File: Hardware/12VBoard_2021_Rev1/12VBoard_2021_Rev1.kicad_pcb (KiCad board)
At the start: 2 copper layers, 101.6 x 129.4 mm, 155 parts, among them Q10 IRLML2060, Q11 IRLML2060, Q12 IRLML2060, Q13 IRLML2060, Q3 IRLML2060, Q8 IRLML2060, Q9 IRLML2060, U1 LT1910, U10 INA198, U11 FDS66900AS, U12 LT1910, U13 INA198, U14 LT1910, U15 LT1910, U16 LT1910, U17 LT1910, U18 FDS66900AS, U19 LT1910, U2 INA198, U20 FDS66900AS, U3 LT1910, U4 LM2576S-12/NOPB, U5 LT1910, U6 LM2576S-12/NOPB, U7 LT1910, U8 INA198, U9 OKI

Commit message: Layout for high current
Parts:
- removed the C13 at (365.6, 106.4)
- removed the C14 at (257.8, 88.3)
- removed the C15 at (283.1, 104.6)
- removed the C15 at (356.7, 66.7)
- removed the C16 at (283.1, 100.1)
- removed the C17 at (361.7, 109.0)
- removed the C17 at (289.4, 85.0)
- removed the C18 at (289.4, 80.5)
- removed the C18 at (356.7, 73.9)
- removed the D1 at (259.9, 104.9)
- removed the R10 at (248.1, 87.8)
- removed the R10 at (343.3, 116.3)
- removed the R13 at (278.8, 104.6)
- removed the R8 at (338.6, 108.5)
- removed the U10 at (269.3, 86.0)
- removed the U10 at (192.5, 65.5)
- removed the U12 at (276.5, 100.1)
- removed the U12 at (235.7, 98.0)
- removed the U7 at (348.0, 109.7)
- added C15: 0.1uF, Capacitor_SMD:C_0603_1608Metric_Pad1.05x0.95mm_HandSolder, F.Cu at (129.2, 21.6)
- added C17: 0.1uF, Capacitor_SMD:C_0603_1608Metric_Pad1.05x0.95mm_HandSolder, F.Cu at (125.5, 26.4)
- added C18: 10uF, Capacitor_THT:CP_Radial_D5.0mm_P2.00mm, F.Cu at (185.7, 65.8)
- added R10: 50m, Package_TO_SOT_THT:TO-126-2_Vertical, F.Cu at (127.5, 35.8)
- added U10: INA198, Package_TO_SOT_SMD:SOT-23-5, F.Cu at (125.8, 41.1)
- added U12: LT1910, Package_SO:SOIC-8-N7_3.9x4.9mm_P1.27mm, F.Cu at (141.4, 56.0)
- D12, D15, R11, R12, R19, R21, R22, R23, U11: moved to F.Cu
- moved R13 262.7 mm to (125.6, 13.0), turned to 0 degrees
- moved R11 248.7 mm to (121.4, 55.3), turned to 270 degrees
- moved R9 234.2 mm to (125.4, 16.5)
- moved C14 224.2 mm to (126.3, 47.5)
- moved C16 222.2 mm to (140.7, 47.5), turned to 0 degrees
- moved C11 218.7 mm to (157.0, 18.8), turned to 90 degrees
- moved TP5 215.4 mm to (147.3, 35.8)
- moved U8 205.9 mm to (148.7, 31.9)
- moved R14 204.4 mm to (153.9, 37.8), turned to 90 degrees
- moved F1 193.2 mm to (150.7, 56.9), turned to 90 degrees
- moved R19 178.9 mm to (119.8, 16.5)
- moved R20 176.2 mm to (119.8, 13.2)
- moved R17 174.2 mm to (120.3, 23.4)
- moved R11 161.1 mm to (120.5, 26.4)
- moved R9 160.4 mm to (120.3, 20.1)
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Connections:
- Conn11 pad 3: Net-(Conn11-Pad3) -> /High Current Outputs/Multimedia/Extra/12V5AMultiMedia
- Conn12 pad 3: Net-(Conn11-Pad3) -> /High Current Outputs/Multimedia/Extra/12V5AMultiMedia
- R18 pad 1: /High Current Outputs/Multimedia/Extra/12V5AMultimedia -> /High Current Outputs/Multimedia/Extra/12V5AMultiMedia
- U20 pad 5: /High Current Outputs/Multimedia/Extra/12V5AMultimedia -> /High Current Outputs/Multimedia/Extra/12V5AMultiMedia
- U20 pad 6: /High Current Outputs/Multimedia/Extra/12V5AMultimedia -> /High Current Outputs/Multimedia/Extra/12V5AMultiMedia
- U20 pad 7: /High Current Outputs/Multimedia/Extra/12V5AMultimedia -> /High Current Outputs/Multimedia/Extra/12V5AMultiMedia
- U20 pad 8: /High Current Outputs/Multimedia/Extra/12V5AMultimedia -> /High Current Outputs/Multimedia/Extra/12V5AMultiMedia
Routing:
- net /High Current Outputs/AuxMount/12VLogicAuxMount: track 44.0 -> 0.00 mm, vias 1 -> 0
- net /High Current Outputs/Gimbal/12VLogicGimbal: track 43.6 -> 0.00 mm, vias 1 -> 0
- net /High Current Outputs/Multimedia/Extra/12VLogicMultiMedia: track 43.0 -> 0.00 mm, vias 1 -> 0
- added copper zone on F.Cu, net /High Current Outputs/AuxMount/12V10AAuxMount
- added copper zone on F.Cu, net /High Current Outputs/AuxMount/12V5AON
- added copper zone on F.Cu, net /High Current Outputs/Gimbal/12V5AGimbal
- added copper zone on F.Cu, net /High Current Outputs/Gimbal/12V5AON
- added copper zone on F.Cu, net /High Current Outputs/Multimedia/Extra/12V5AMultiMedia
- added copper zone on F.Cu, net Net-(F1-Pad2)
- added copper zone on F.Cu, net Net-(F3-Pad2)
- added copper zone on F.Cu, net Net-(F4-Pad2)
- added copper zone on F.Cu, net Net-(R11-Pad2)
- added copper zone on F.Cu, net Net-(R17-Pad2)

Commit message: did planes for high current
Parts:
- removed the R11 at (120.5, 26.4)
- removed the R17 at (120.3, 23.4)
- removed the R19 at (125.6, 18.5)
- removed the R20 at (171.6, 66.3)
- removed the R20 at (119.8, 13.2)
- removed the R9 at (120.3, 20.1)
- added R20: 0.01, Resistor_SMD:R_0603_1608Metric_Pad1.05x0.95mm_HandSolder, F.Cu at (153.4, 54.7)
- moved R19 71.3 mm to (173.6, 63.2)
- moved C17 62.5 mm to (173.6, 66.3)
- moved R13 45.8 mm to (146.7, 53.6)
- moved R9 45.5 mm to (127.9, 62.0)
- moved C13 35.6 mm to (126.6, 58.9)
- moved C15 34.5 mm to (146.7, 51.3)
- moved U19 13.3 mm to (166.0, 65.2), turned to 180 degrees
- moved U20 12.5 mm to (153.3, 61.7), turned to 270 degrees
- moved R14 10.8 mm to (151.1, 27.4), turned to 180 degrees
- moved F1 10.4 mm to (151.3, 46.5)
- moved C18 6.87 mm to (178.8, 65.0)
- moved F2 6.60 mm to (185.4, 18.9)
- moved C10 4.80 mm to (193.3, 17.3), turned to 0 degrees
- moved C11 3.34 mm to (153.7, 19.3), turned to 270 degrees
- moved F3 3.05 mm to (132.7, 46.2)
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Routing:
- added copper zone on B.Cu, net /High Current Outputs/12VActuation
- added copper zone on B.Cu, net Net-(C10-Pad1)

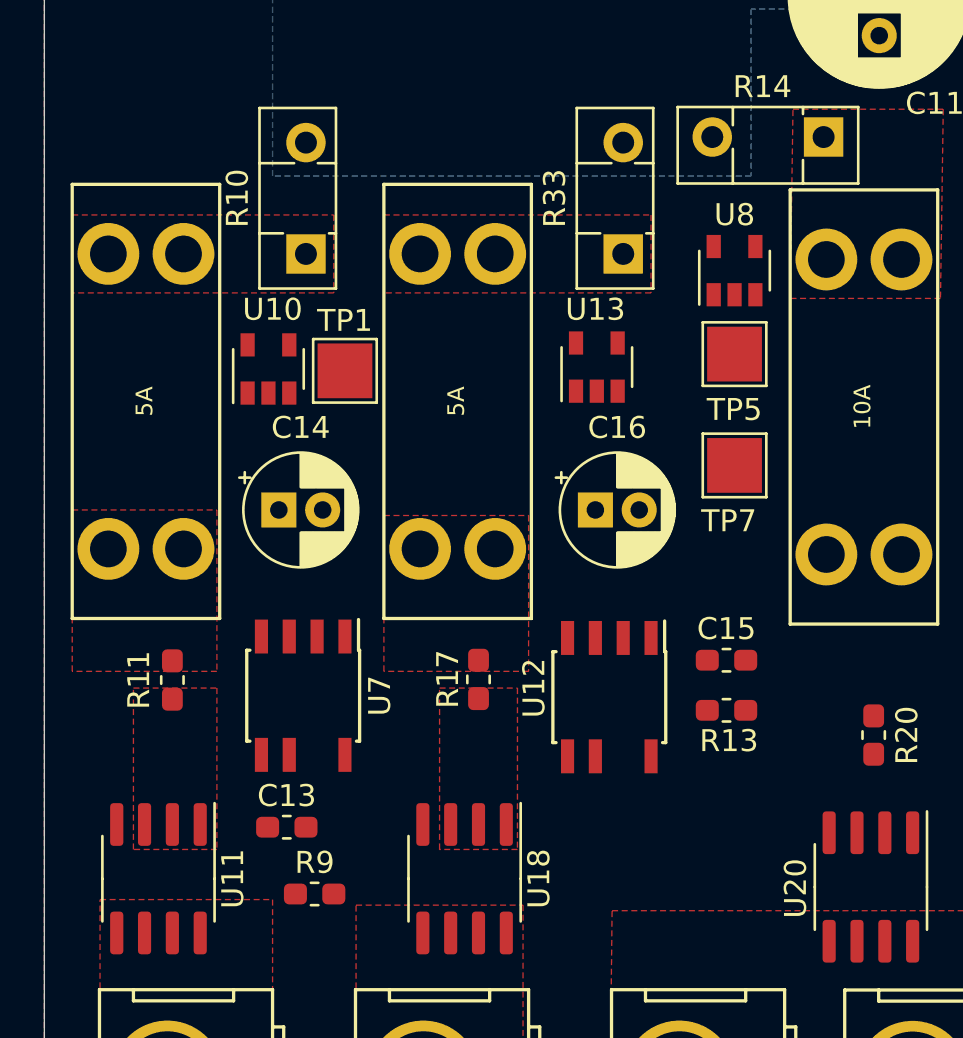
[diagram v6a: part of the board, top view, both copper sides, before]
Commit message: Routing of mosfet drivers and current sensors
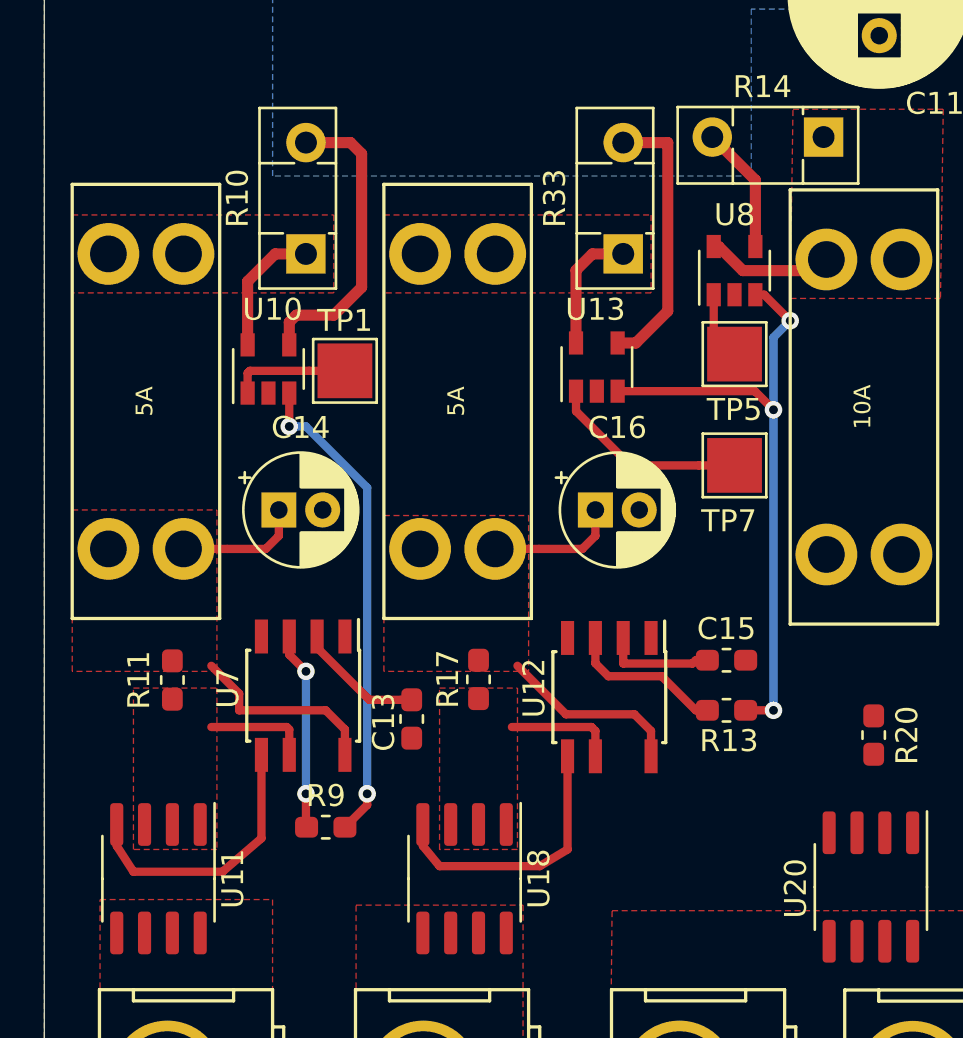
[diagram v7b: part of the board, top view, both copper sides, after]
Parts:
- moved C13 7.54 mm to (132.3, 54.0), turned to 270 degrees
- moved R9 3.09 mm to (128.4, 58.9)
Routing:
- net +5V: track 194.6 -> 245.7 mm, vias 7 -> 12
- net /High Current Outputs/AuxMount/12V5AON: track 0.00 -> 14.7 mm
- net /High Current Outputs/Gimbal/12V5AON: track 0.00 -> 14.5 mm
- net /High Current Outputs/AuxMount/12Actuation: track 0.00 -> 13.8 mm
- net /High Current Outputs/Gimbal/12Actuation: track 0.00 -> 12.6 mm
- net Net-(U11-Pad4): track 0.00 -> 12.6 mm
- net Net-(U12-Pad5): track 0.00 -> 12.5 mm
- net /High Current Outputs/GimbalSense: track 0.00 -> 9.17 mm
- net Net-(R9-Pad1): track 0.00 -> 9.03 mm, vias 0 -> 2
- net Net-(R13-Pad1): track 0.00 -> 7.15 mm
- net Net-(F4-Pad2): track 0.00 -> 6.08 mm
- net Net-(C13-Pad1): track 0.00 -> 5.81 mm
- net /High Current Outputs/Multimedia/Extra/12Actuation: track 0.00 -> 5.81 mm
- net Net-(F1-Pad2): track 0.00 -> 5.81 mm
- net Net-(F3-Pad2): track 0.00 -> 5.78 mm
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
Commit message: LED work, started on control signals
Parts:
- removed the D12 at (241.9, 104.4)
- removed the R12 at (238.4, 104.5)
- moved D12 122.1 mm to (119.9, 93.1), turned to 0 degrees
- moved D13 118.6 mm to (119.9, 96.4)
- moved R21 118.4 mm to (123.7, 96.4)
- moved R12 114.8 mm to (123.7, 93.1), turned to 180 degrees
- moved D15 111.7 mm to (130.8, 96.3)
- moved R22 104.1 mm to (134.8, 96.3), turned to 180 degrees
- moved D1 86.2 mm to (152.2, 92.8)
- moved R8 86.0 mm to (155.9, 92.8)
- moved R23 25.8 mm to (145.7, 96.1), turned to 180 degrees
- moved D16 18.6 mm to (142.0, 96.1), turned to 0 degrees
- moved D14 5.11 mm to (142.0, 93.2), turned to 0 degrees
- moved D18 4.42 mm to (130.8, 93.1), turned to 0 degrees
- moved R34 3.06 mm to (134.7, 93.1), turned to 180 degrees
- moved R18 2.20 mm to (145.7, 93.2), turned to 180 degrees
- moved R20 0.51 mm to (153.9, 54.7)
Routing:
- net +5V: track 245.7 -> 319.9 mm, vias 12 -> 14
- net /High Current Outputs/Multimedia/Extra/12VLogicMultiMedia: track 0.00 -> 63.5 mm, vias 0 -> 2
- net /High Current Outputs/AuxMountCTL_Log: track 0.00 -> 61.4 mm, vias 0 -> 3
- net /High Current Outputs/Gimbal/12VLogicGimbal: track 0.00 -> 60.7 mm, vias 0 -> 2
- net /High Current Outputs/AuxMount/12VLogicAuxMount: track 0.00 -> 60.1 mm, vias 0 -> 2
- net /High Current Outputs/GimbalCTL_Log: track 0.00 -> 52.7 mm
- net /High Current Outputs/Multimedia/Extra/12V5AON: track 0.00 -> 36.4 mm, vias 0 -> 2
- net /High Current Outputs/MultiMediaCTL_Log: track 0.00 -> 29.4 mm
- net /High Current Outputs/Multimedia/Extra/12V5AMultiMedia: track 0.00 -> 24.8 mm
- net /High Current Outputs/AuxMount/12V10AAuxMount: track 0.00 -> 24.2 mm
- net /High Current Outputs/Gimbal/12V5AGimbal: track 0.00 -> 24.1 mm
- net Net-(U19-Pad5): track 0.00 -> 14.5 mm
- net /High Current Outputs/12VLogic: track 107.9 -> 122.3 mm
- net Net-(R20-Pad2): track 0.00 -> 10.3 mm, vias 0 -> 2
- net Net-(Q3-Pad3): track 4.44 -> 12.1 mm
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- added copper zone on F.Cu, net /High Current Outputs/Multimedia/Extra/12V5AON
- added copper zone on F.Cu, net Net-(R20-Pad2)
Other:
- board text added: "12V Logic"
- board text added: "ACT"
- board text added: "LOG"
